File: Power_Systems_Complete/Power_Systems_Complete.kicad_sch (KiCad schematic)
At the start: 0 parts

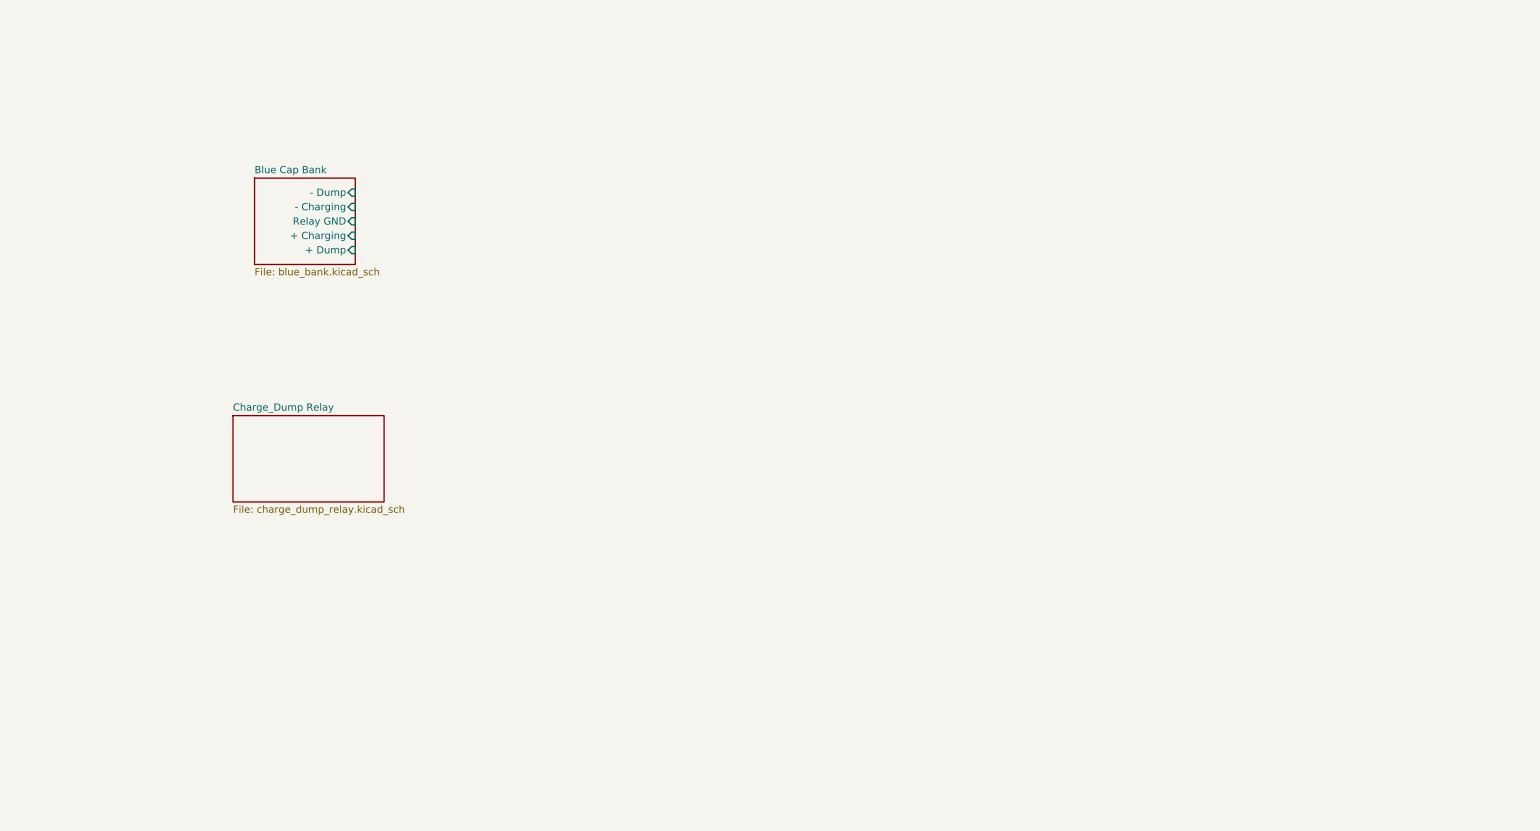
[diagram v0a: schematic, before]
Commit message: Added SPA to complete schematic
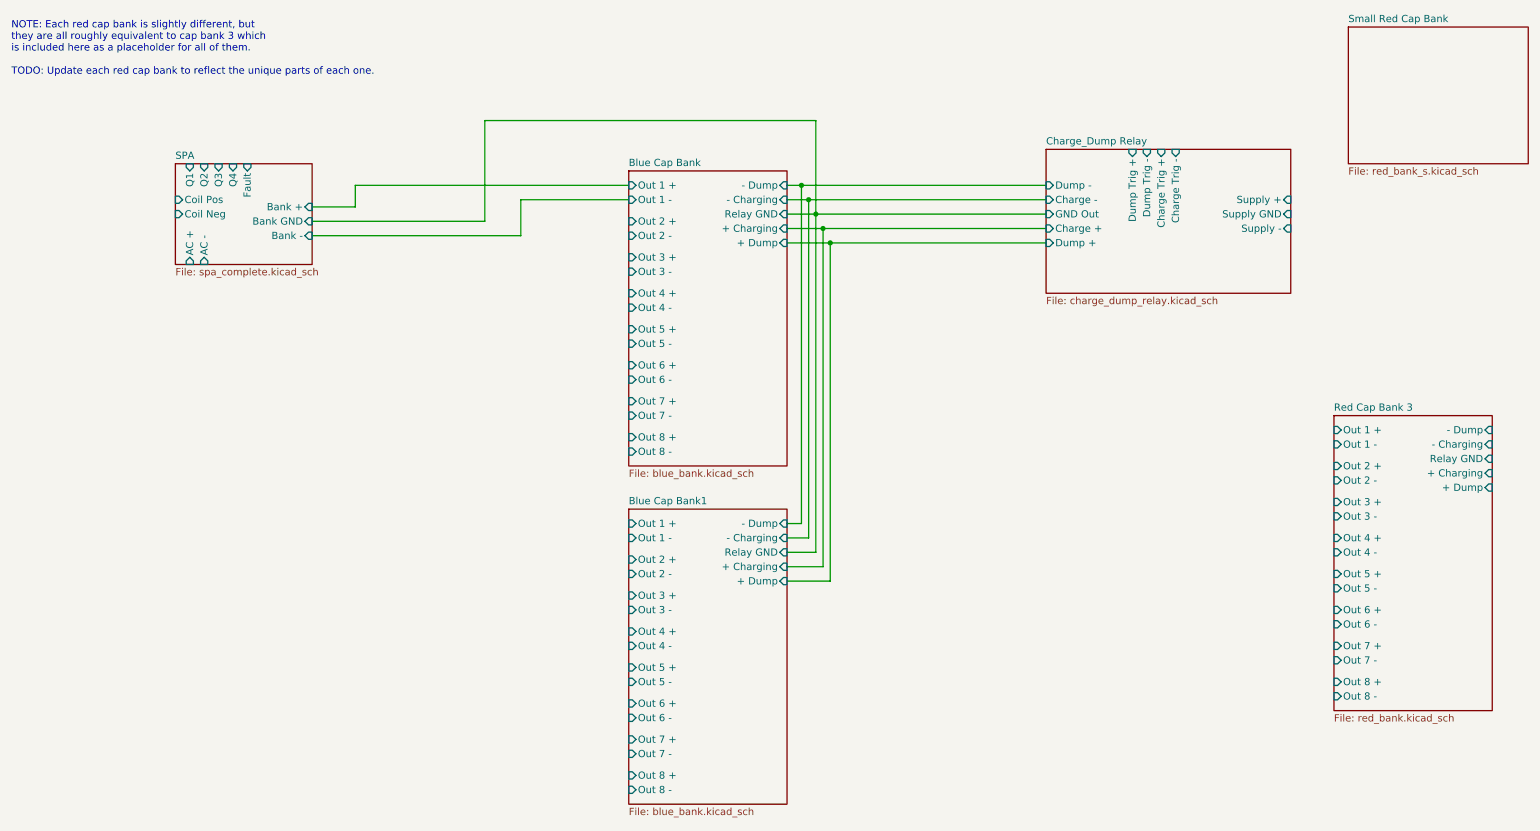
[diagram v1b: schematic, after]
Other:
- added sheet Blue Cap Bank1 (blue_bank.kicad_sch)
- added sheet Red Cap Bank 3 (red_bank.kicad_sch)
- added sheet SPA (spa_complete.kicad_sch)
- added sheet Small Red Cap Bank (red_bank_s.kicad_sch)
- sheet Blue Cap Bank ports: added Out 1 +, Out 1 -, Out 2 +, Out 2 -, Out 3 +, Out 3 -, Out 4 +, Out 4 -, Out 5 +, Out 5 -, Out 6 +, Out 6 -, Out 7 +, Out 7 -, Out 8 +, Out 8 -; removed none
- sheet Charge_Dump Relay ports: added Charge +, Charge -, Charge Trig +, Charge Trig -, Dump +, Dump -, Dump Trig +, Dump Trig -, GND Out, Supply +, Supply -, Supply GND; removed none
- note added: "NOTE: Each red cap bank is slightly different, but they are all roughly equivalent to cap bank 3 which is included here as a placeholder for all of them. TODO: Update each red cap bank to reflect the unique parts of each one."

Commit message: completed tf and pf
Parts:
- added AC?: ~, symbol DIY_ICs:AC_Input
- added C? (x29): C, symbol Device:C
- added L? (x59): L, symbol Device:L
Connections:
- net SPA0/AC +: now also AC?.1
- net SPA0/AC -: now also AC?.2
- net SPA0/Coil Neg: now also C?.2, L?.2, L?.2
- net SPA0/Coil Pos: now also L?.2
- new net: C?.1, L?.1, L?.1 (x28)
- new net: C?.1, L?.1, L?.1, L?.1
- new net SPA32/Coil Neg: C?.2, L?.2
- new net SPA32/Coil Pos: L?.2
- new net SPA33/Coil Neg: C?.2, L?.2
- new net SPA33/Coil Pos: L?.2
- new net SPA34/Coil Neg: C?.2, L?.2
- new net SPA34/Coil Pos: L?.2
- new net SPA35/Coil Neg: C?.2, L?.2
- new net SPA35/Coil Pos: L?.2
- new net SPA36/Coil Neg: C?.2, L?.2
- new net SPA36/Coil Pos: L?.2
- new net SPA37/Coil Neg: C?.2, L?.2
- new net SPA37/Coil Pos: L?.2
- new net SPA38/Coil Neg: C?.2, L?.2
- new net SPA38/Coil Pos: L?.2
- new net SPA39/Coil Neg: C?.2, L?.2
- new net SPA39/Coil Pos: L?.2
- new net SPA40/Coil Neg: C?.2, L?.2
- new net SPA40/Coil Pos: L?.2
- new net SPA41/Coil Neg: C?.2, L?.2
- new net SPA41/Coil Pos: L?.2
- new net SPA42/Coil Neg: C?.2, L?.2
- new net SPA42/Coil Pos: L?.2
- new net SPA43/Coil Neg: C?.2, L?.2
- new net SPA43/Coil Pos: L?.2
- new net SPA44/Coil Neg: C?.2, L?.2
- new net SPA44/Coil Pos: L?.2
- new net SPA45/Coil Neg: C?.2, L?.2
- new net SPA45/Coil Pos: L?.2
- new net SPA46/Coil Neg: C?.2, L?.2
- new net SPA46/Coil Pos: L?.2
- new net SPA47/Coil Neg: C?.2, L?.2
- new net SPA47/Coil Pos: L?.2
- new net SPA48/Coil Neg: C?.2, L?.2
- new net SPA48/Coil Pos: L?.2
- new net SPA49/Coil Neg: C?.2, L?.2
- new net SPA49/Coil Pos: L?.2
- new net SPA50/Coil Neg: C?.2, L?.2
- new net SPA50/Coil Pos: L?.2
- new net SPA51/Coil Neg: C?.2, L?.2
- new net SPA51/Coil Pos: L?.2
- new net SPA52/Coil Neg: C?.2, L?.2
- new net SPA52/Coil Pos: L?.2
- new net SPA53/Coil Neg: C?.2, L?.2
- new net SPA53/Coil Pos: L?.2
- new net SPA54/Coil Neg: C?.2, L?.2
- new net SPA54/Coil Pos: L?.2
- new net SPA55/Coil Neg: C?.2, L?.2
- new net SPA55/Coil Pos: L?.2
- new net SPA56/Coil Neg: C?.2, L?.2
- new net SPA56/Coil Pos: L?.2
- new net SPA57/Coil Neg: C?.2, L?.2
- new net SPA57/Coil Pos: L?.2
- new net SPA58/Coil Neg: C?.2, L?.2
- new net SPA58/Coil Pos: L?.2
- new net SPA59/Coil Neg: C?.2, L?.2
- new net SPA59/Coil Pos: L?.2
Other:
- sheet Blue Cap Bank renamed Blue Cap Bank0
- sheet Red Cap Bank 3 renamed Red Cap Bank 3_
- sheet SPA renamed SPA0
- removed sheet Small Red Cap Bank
- added sheet Blue Cap Bank2 (blue_bank.kicad_sch)
- added sheet Blue Cap Bank3 (blue_bank.kicad_sch)
- added sheet Red Cap Bank 3_1 (red_bank.kicad_sch)
- added sheet Red Cap Bank 3_2 (red_bank.kicad_sch)
- added sheet SPA1 (spa_complete.kicad_sch)
- added sheet SPA10 (spa_complete.kicad_sch)
- added sheet SPA11 (spa_complete.kicad_sch)
- added sheet SPA12 (spa_complete.kicad_sch)
- added sheet SPA13 (spa_complete.kicad_sch)
- added sheet SPA14 (spa_complete.kicad_sch)
- added sheet SPA15 (spa_complete.kicad_sch)
- added sheet SPA16 (spa_complete.kicad_sch)
- added sheet SPA17 (spa_complete.kicad_sch)
- added sheet SPA18 (spa_complete.kicad_sch)
- added sheet SPA19 (spa_complete.kicad_sch)
- added sheet SPA2 (spa_complete.kicad_sch)
- added sheet SPA20 (spa_complete.kicad_sch)
- added sheet SPA21 (spa_complete.kicad_sch)
- added sheet SPA22 (spa_complete.kicad_sch)
- added sheet SPA23 (spa_complete.kicad_sch)
- added sheet SPA24 (spa_complete.kicad_sch)
- added sheet SPA25 (spa_complete.kicad_sch)
- added sheet SPA26 (spa_complete.kicad_sch)
- added sheet SPA27 (spa_complete.kicad_sch)
- added sheet SPA28 (spa_complete.kicad_sch)
- added sheet SPA29 (spa_complete.kicad_sch)
- added sheet SPA3 (spa_complete.kicad_sch)
- added sheet SPA32 (spa_complete.kicad_sch)
- added sheet SPA33 (spa_complete.kicad_sch)
- added sheet SPA34 (spa_complete.kicad_sch)
- added sheet SPA35 (spa_complete.kicad_sch)
- added sheet SPA36 (spa_complete.kicad_sch)
- added sheet SPA37 (spa_complete.kicad_sch)
- added sheet SPA38 (spa_complete.kicad_sch)
- added sheet SPA39 (spa_complete.kicad_sch)
- added sheet SPA4 (spa_complete.kicad_sch)
- added sheet SPA40 (spa_complete.kicad_sch)
- added sheet SPA41 (spa_complete.kicad_sch)
- added sheet SPA42 (spa_complete.kicad_sch)
- added sheet SPA43 (spa_complete.kicad_sch)
- added sheet SPA44 (spa_complete.kicad_sch)
- added sheet SPA45 (spa_complete.kicad_sch)
- added sheet SPA46 (spa_complete.kicad_sch)
- added sheet SPA47 (spa_complete.kicad_sch)
- added sheet SPA48 (spa_complete.kicad_sch)
- added sheet SPA49 (spa_complete.kicad_sch)
- added sheet SPA5 (spa_complete.kicad_sch)
- added sheet SPA50 (spa_complete.kicad_sch)
- added sheet SPA51 (spa_complete.kicad_sch)
- added sheet SPA52 (spa_complete.kicad_sch)
- added sheet SPA53 (spa_complete.kicad_sch)
- added sheet SPA54 (spa_complete.kicad_sch)
- added sheet SPA55 (spa_complete.kicad_sch)
- added sheet SPA56 (spa_complete.kicad_sch)
- added sheet SPA57 (spa_complete.kicad_sch)
- added sheet SPA58 (spa_complete.kicad_sch)
- added sheet SPA59 (spa_complete.kicad_sch)
- added sheet SPA6 (spa_complete.kicad_sch)
- added sheet SPA7 (spa_complete.kicad_sch)
- added sheet SPA8 (spa_complete.kicad_sch)
- added sheet SPA9 (spa_complete.kicad_sch)
- sheet Blue Cap Bank0 ports: added Out 10 +, Out 10 -, Out 9 +, Out 9 -; removed none
- sheet Blue Cap Bank1 ports: added Out 10 +, Out 10 -, Out 9 +, Out 9 -; removed none
- note added: "Actually red bank 1"
- note added: "Actually red bank 2"
- note added: "CC 01 PF Coil"
- note added: "CC 02 PF Coil"
- note added: "CC 03 PF Coil"
- note added: "CC 04 PF Coil"
- note added: "CC 05 PF Coil"
- note added: "CC 06 PF Coil"
- note added: "CC 07 PF Coil"
- note added: "CC 08 PF Coil"
- note added: "CC 09 PF Coil"
- note added: "CC 10 PF Coil"
- note added: "CS 01 PF Coil"
- note added: "CS 02 PF Coil"
- note added: "CS 03 PF Coil"
- note added: "CS 04 PF Coil"
- note added: "CS 05 PF Coil"
- note added: "CS 06 PF Coil"
- note added: "CS 07 PF Coil"
- note added: "CS 08 PF Coil"
- note added: "CS 09 PF Coil"
- note added: "CS 10 PF Coil"
- note added: "CS 11 PF Coil"
- note added: "CS 12 PF Coil"
- note added: "CS 13 PF Coil"
- note added: "CS 14 PF Coil"
- note added: "LC Tank"
- note added: "TF Coil"
- note added: "TODO: Fix numbering of PF coil labels"

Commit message: Completed wiring for TF
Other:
- added sheet Charge_Dump Relay1 (charge_dump_relay.kicad_sch)

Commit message: Fixed SPA ordering
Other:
- added sheet SPA30 (spa_complete.kicad_sch)
- added sheet SPA31 (spa_complete.kicad_sch)
- moved on the sheet: C?, L?

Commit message: Made changes
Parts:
- added AC?: ~, symbol DIY_ICs:AC_Input
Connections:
- net Blue Cap Bank3/Relay GND: now also AC?.2
- net SPA32/AC +: now also AC?.1
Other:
- added sheet Fiber Optic Driver (fo_driver.kicad_sch)
- note added: "CC 11 PF Coil"
- note added: "CC 12 PF Coil"
- note added: "CC 13 PF Coil"
- note added: "CC 14 PF Coil"

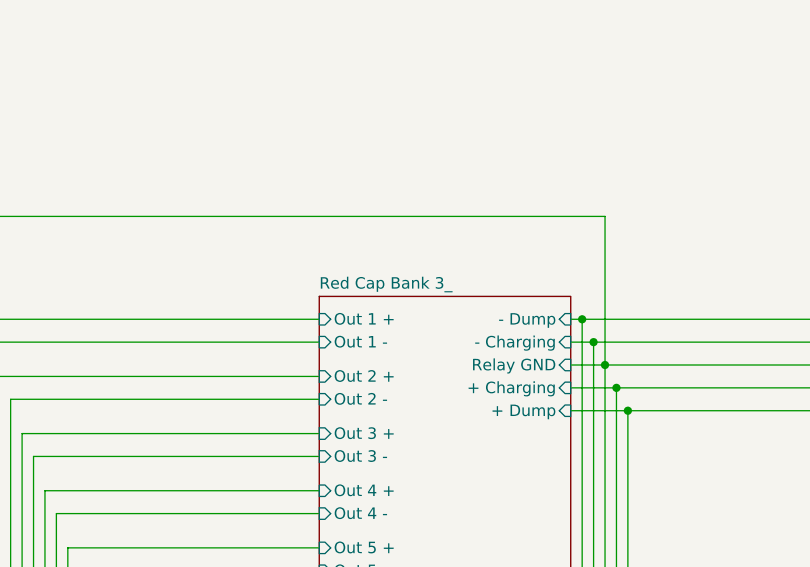
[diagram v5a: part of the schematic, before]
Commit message: Edited red cap bank 1 caps
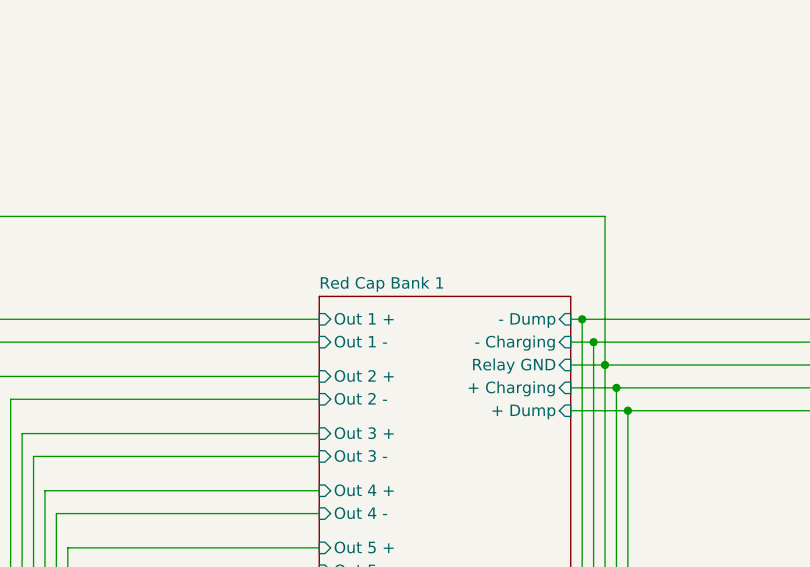
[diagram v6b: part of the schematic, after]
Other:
- sheet Red Cap Bank 3_ renamed Red Cap Bank 1
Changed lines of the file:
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@@
 			(color 0 0 0 0.0000)
 		)
-		(property "Sheetname" "Red Cap Bank 3_"
+		(property "Sheetname" "Red Cap Bank 1"
 			(at 312.42 103.4284 0)
 			(effects
